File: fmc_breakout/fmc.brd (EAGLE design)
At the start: 101 x 62.3 mm, 19 parts

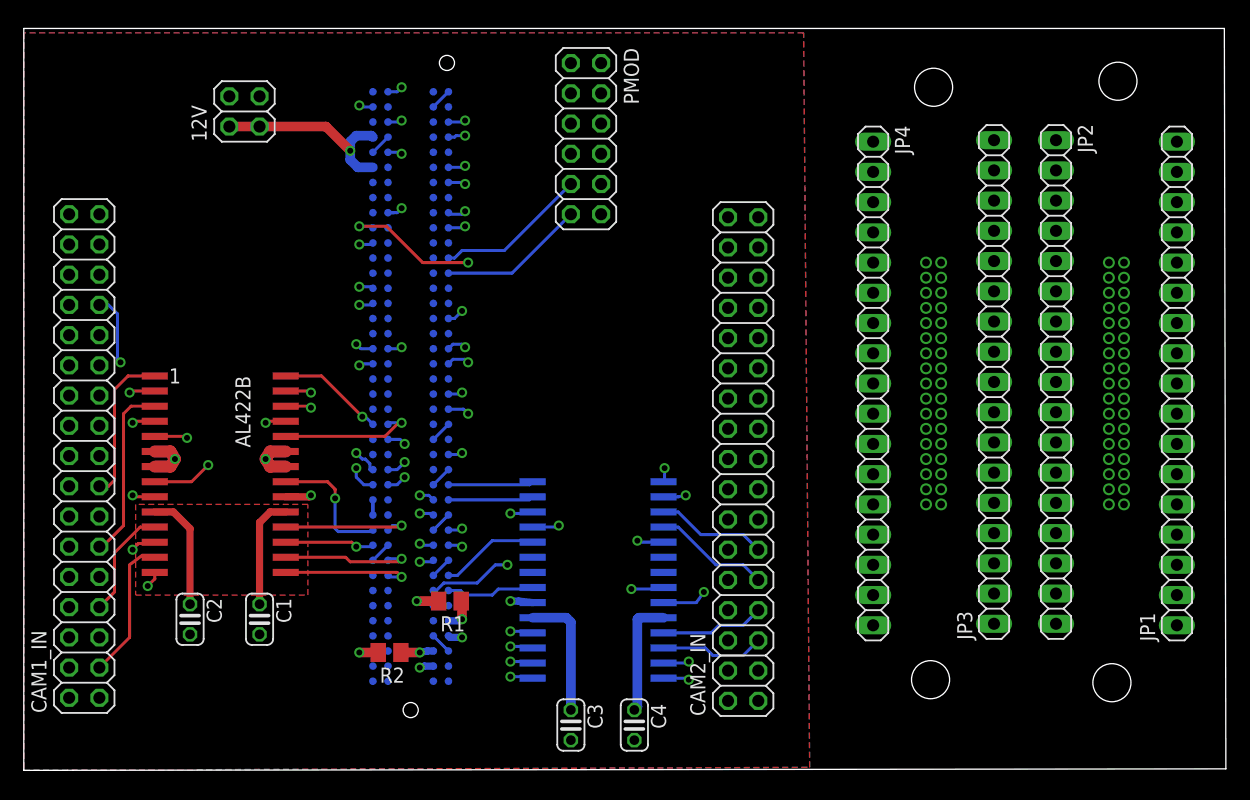
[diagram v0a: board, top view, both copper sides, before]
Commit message: Finished routing traces
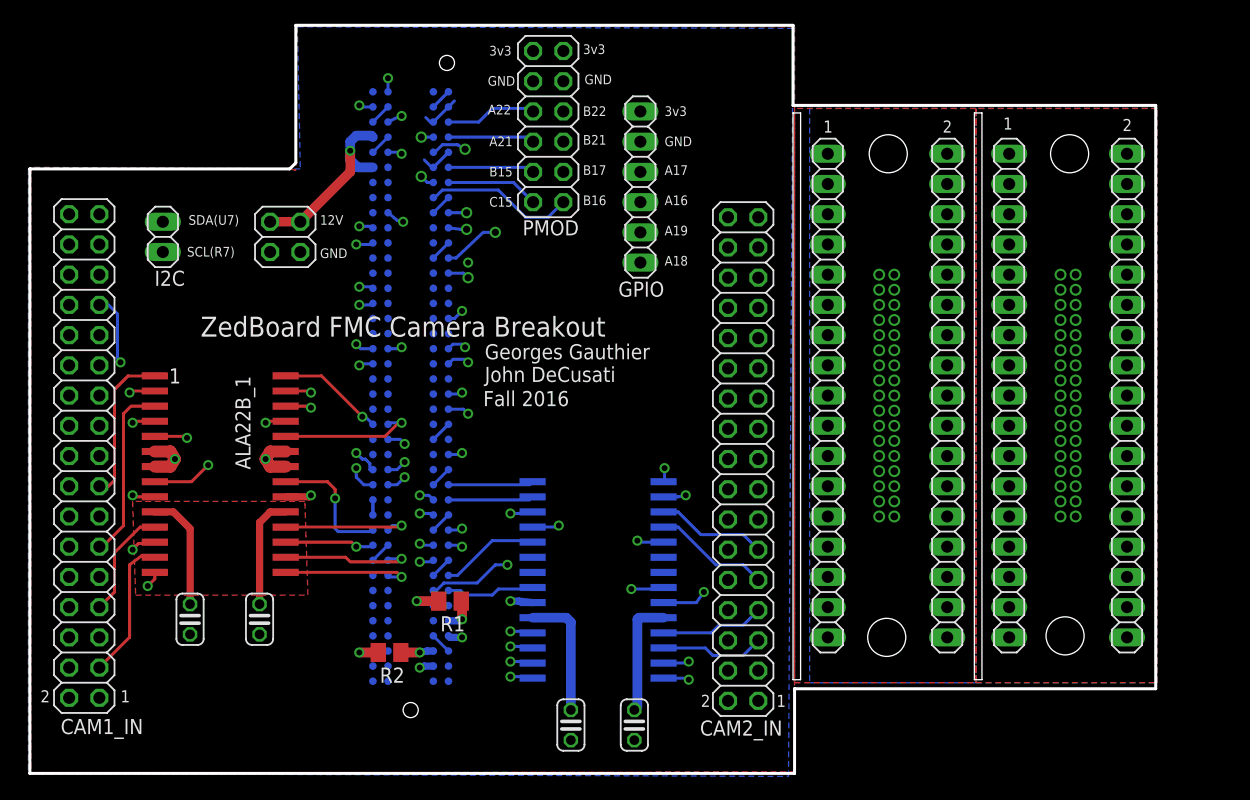
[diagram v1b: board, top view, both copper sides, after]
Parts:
- removed 12V: (no value), pinhead:2X02
- added GPIO: (no value), pinhead:1X06
- added I2C: (no value), pinhead:1X02
- added PWR: PWR, pinhead:2X02
- moved JP1 14.1 mm to (85.3, 36.8), turned to 270 degrees
- moved JP2 6.08 mm to (95.2, 36.8), turned to 90 degrees
- moved CAM1 4.19 mm to (90.3, 36.8), turned to 90 degrees
- moved JP3 4.10 mm to (80.1, 36.8)
- moved CAM2 4.07 mm to (75.1, 36.8)
- moved JP4 3.94 mm to (70.1, 36.8)
- moved PMOD 3.33 mm to (46.6, 59.4)
- renumbered AL422B to ALA22B_1, U$2 to AL422B_2
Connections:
- net 12V: now also PWR.1, PWR.2; no longer 12V.1, 12V.2
- net 3V3: now also GPIO.6
- net A16: now also GPIO.3; no longer PMOD.7
- net A17: now also GPIO.4; no longer PMOD.5
- net A18: now also GPIO.1; no longer PMOD.11
- net A19: now also GPIO.2; no longer PMOD.9
- net A21: now also PMOD.7; no longer PMOD.8
- net A22: now also PMOD.5; no longer PMOD.6
- net B15: now also PMOD.9; no longer PMOD.10
- net B16: now also PMOD.12
- net B17: now also PMOD.10
- net B21: now also PMOD.8
- net B22: now also PMOD.6
- net C15: now also PMOD.11; no longer PMOD.12
- net GND: now also GPIO.5, PWR.3, PWR.4; no longer 12V.3, 12V.4
- net N$40: now also CAM2.25
- net N$60: now also CAM2.20
- net SCL(R7): now also I2C.1
- net SDA(U7): now also I2C.2
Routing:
- net B17: track 0.00 -> 14.1 mm, vias 0 -> 1
- net B22: track 0.00 -> 13.8 mm, vias 0 -> 1
- net N$18: track 0.00 -> 13.0 mm
- net N$1: track 0.00 -> 12.9 mm
- net N$69: track 0.00 -> 12.8 mm
- net N$53: track 0.00 -> 12.8 mm
- net N$35: track 0.00 -> 12.8 mm
- net N$17: track 0.00 -> 12.8 mm
- net N$52: track 0.00 -> 12.7 mm
- net B16: track 0.00 -> 12.7 mm
- net N$19: track 0.00 -> 12.7 mm
- net N$36: track 0.00 -> 12.5 mm
- net N$54: track 0.00 -> 12.4 mm
- net N$34: track 0.00 -> 12.3 mm
- net N$37: track 0.00 -> 12.3 mm
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- added copper zone on layer 1, net N$76
- added copper zone on layer 16, net N$77
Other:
- board size 101 x 62.3 mm -> 94.6 x 62.9 mm
- board text added: "1"
- board text added: "12V"
- board text added: "2"
- board text added: "3v3"
- board text added: "A16"
- board text added: "A17"
- board text added: "A18"
- board text added: "A19"
- board text added: "A21"
- board text added: "A22"
- board text added: "B15"
- board text added: "B16"
- board text added: "B17"
- board text added: "B21"
- board text added: "B22"
- board text added: "C15"
- board text added: "Fall 2016"
- board text added: "GND"
- board text added: "Georges Gauthier"
- board text added: "John DeCusati"
- board text added: "SCL(R7)"
- board text added: "SDA(U7)"
- board text added: "ZedBoard FMC Camera Breakout"

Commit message: FMC board tweaks
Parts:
- moved R2 0.25 mm to (33.3, 15.0)
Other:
- board size 94.6 x 62.9 mm -> 94.6 x 62.1 mm
- board text added: "For LI-VM34LP camera modules & AL422b FIFOs"
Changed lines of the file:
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@@
 <layers>
 <layer number="1" name="Top" color="4" fill="1" visible="yes" active="yes"/>
-<layer number="2" name="Route2" color="13" fill="1" visible="yes" active="yes"/>
+<layer number="2" name="Route2" color="14" fill="1" visible="yes" active="yes"/>
 <layer number="3" name="Route3" color="4" fill="3" visible="no" active="no"/>
 <layer number="14" name="Route14" color="1" fill="6" visible="no" active="no"/>
@@
 <layer number="25" name="tNames" color="7" fill="1" visible="yes" active="yes"/>
 <layer number="26" name="bNames" color="7" fill="1" visible="yes" active="yes"/>
-<layer number="27" name="tValues" color="7" fill="1" visible="yes" active="yes"/>
-<layer number="28" name="bValues" color="7" fill="1" visible="yes" active="yes"/>
+<layer number="27" name="tValues" color="7" fill="1" visible="no" active="yes"/>
+<layer number="28" name="bValues" color="7" fill="1" visible="no" active="yes"/>
 <layer number="29" name="tStop" color="7" fill="3" visible="no" active="yes"/>
 <layer number="30" name="bStop" color="7" fill="6" visible="no" active="yes"/>
@@
 <board>
 <plain>
-<hole x="90.043" y="16.637" drill="3.2"/>
-<hole x="75.184" y="57.15" drill="3.2"/>
-<hole x="75.057" y="16.51" drill="3.2"/>
-<hole x="90.424" y="57.15" drill="3.2"/>
-<wire x1="67.31" y1="5.08" x2="67.31" y2="12.192" width="0.254" layer="20"/>
+<hole x="90.297" y="14.605" drill="3.2"/>
+<hole x="75.184" y="58.674" drill="3.2"/>
+<hole x="75.057" y="14.478" drill="3.2"/>
+<hole x="90.424" y="58.674" drill="3.2"/>
+<wire x1="67.31" y1="5.842" x2="67.31" y2="12.192" width="0.254" layer="20"/>
 <wire x1="67.31" y1="12.192" x2="97.663" y2="12.192" width="0.254" layer="20"/>
 <wire x1="97.663" y1="12.192" x2="97.663" y2="61.214" width="0.254" layer="20"/>
@@
 <text x="27.432" y="51.181" size="0.8128" layer="25" ratio="10">12V</text>
 <text x="27.432" y="48.387" size="0.8128" layer="25" ratio="10">GND</text>
-<text x="41.148" y="35.941" size="1.27" layer="25" ratio="10">Fall 2016</text>
+<text x="41.402" y="35.941" size="1.27" layer="25" ratio="10">Fall 2016</text>
 <text x="10.668" y="11.049" size="1.016" layer="25" ratio="10">1</text>
 <text x="3.937" y="11.049" size="1.016" layer="25" ratio="10">2</text>
 <text x="59.436" y="10.668" size="1.016" layer="25" ratio="10">2</text>
 <text x="65.786" y="10.668" size="1.016" layer="25" ratio="10">1</text>
-<text x="69.723" y="58.928" size="1.016" layer="25" ratio="10">1</text>
-<text x="84.836" y="59.182" size="1.016" layer="25" ratio="10">1</text>
-<text x="79.756" y="58.928" size="1.016" layer="25" ratio="10">2</text>
-<text x="94.869" y="59.055" size="1.016" layer="25" ratio="10">2</text>
+<text x="69.723" y="13.716" size="1.016" layer="25" ratio="10">1</text>
+<text x="85.09" y="13.716" size="1.016" layer="25" ratio="10">1</text>
+<text x="79.756" y="13.716" size="1.016" layer="25" ratio="10">2</text>
+<text x="94.869" y="13.589" size="1.016" layer="25" ratio="10">2</text>
 <wire x1="67.183" y1="67.945" x2="25.4" y2="67.945" width="0.254" layer="20"/>
 <wire x1="25.4" y1="67.945" x2="25.4" y2="56.388" width="0.254" layer="20"/>
 <wire x1="25.4" y1="56.388" x2="24.892" y2="55.88" width="0.254" layer="20"/>
 <wire x1="24.892" y1="55.88" x2="3.048" y2="55.88" width="0.254" layer="20"/>
-<wire x1="3.048" y1="54.356" x2="3.048" y2="5.08" width="0.254" layer="20"/>
-<wire x1="67.31" y1="5.08" x2="3.048" y2="5.08" width="0.254" layer="20"/>
+<wire x1="3.048" y1="54.356" x2="3.048" y2="5.842" width="0.254" layer="20"/>
+<wire x1="67.31" y1="5.842" x2="3.048" y2="5.842" width="0.254" layer="20"/>
 <wire x1="3.048" y1="54.483" x2="3.048" y2="55.88" width="0.254" layer="20"/>
 <text x="16.256" y="48.514" size="0.8128" layer="25" ratio="10">SCL(R7)</text>
+<text x="12.7" y="7.112" size="0.8128" layer="25" ratio="10">For LI-VM34LP camera modules &amp; AL422b FIFOs</text>
 </plain>
 <attributes>
@@
 <attribute name="VALUE" x="51.181" y="12.192" size="1.27" layer="27" ratio="10" rot="R270"/>
 </element>
-<element name="CAM1" library="_hhn_con_pinhead_box_1mm27" package="PHB_1MM27_2X17_SNT" value="" x="90.297" y="36.83" rot="MR90"/>
-<element name="CAM2" library="_hhn_con_pinhead_box_1mm27" package="PHB_1MM27_2X17_SNT" value="" x="75.057" y="36.83" rot="MR90"/>
+<element name="CAM1" library="_hhn_con_pinhead_box_1mm27" package="PHB_1MM27_2X17_SNT" value="" x="90.297" y="36.83" smashed="yes" rot="MR90">
+<attribute name="NAME" x="92.4401" y="20.8439" size="1.27" layer="26" ratio="9" rot="MR0"/>
+<attribute name="VALUE" x="94.5038" y="51.5144" size="1.27" layer="28" ratio="9" rot="MR270"/>
+</element>
+<element name="CAM2" library="_hhn_con_pinhead_box_1mm27" package="PHB_1MM27_2X17_SNT" value="" x="75.057" y="36.83" smashed="yes" rot="MR90">
+<attribute name="NAME" x="77.4541" y="20.8439" size="1.27" layer="26" ratio="9" rot="MR0"/>
+<attribute name="VALUE" x="79.2638" y="51.5144" size="1.27" layer="28" ratio="9" rot="MR270"/>
+</element>
 <element name="JP1" library="pinhead" package="1X17" value="" x="85.344" y="36.83" smashed="yes" rot="R270">
 <attribute name="VALUE" x="82.169" y="58.42" size="1.27" layer="27" rot="R270"/>
@@
 <attribute name="VALUE" x="42.164" y="67.056" size="1.27" layer="27" rot="R270"/>
 </element>
-<element name="R1" library="resistor" package="M0805" value="" x="38.354" y="19.558" rot="R180"/>
-<element name="R2" library="resistor" package="M0805" value="" x="33.274" y="15.24" rot="R180"/>
+<element name="R1" library="resistor" package="M0805" value="" x="38.354" y="19.558" smashed="yes" rot="R180">
+<attribute name="NAME" x="39.624" y="21.844" size="1.27" layer="25" rot="R180"/>
+<attribute name="VALUE" x="39.624" y="22.098" size="1.27" layer="27" rot="R180"/>
+</element>
+<element name="R2" library="resistor" package="M0805" value="" x="33.274" y="14.986" rot="R180"/>
 <element name="I2C" library="pinhead" package="1X02" value="" x="14.224" y="50.165" smashed="yes" rot="R90">
 <attribute name="NAME" x="16.0782" y="47.3202" size="1.27" layer="25" ratio="10" rot="R180"/>
@@
 <wire x1="37.404" y1="19.558" x2="35.56" y2="19.558" width="0.8128" layer="1"/>
 <via x="35.56" y="19.558" extent="1-16" drill="0.5" shape="octagon"/>
-<wire x1="32.324" y1="15.24" x2="30.734" y2="15.24" width="0.8128" layer="1"/>
-<via x="30.734" y="15.24" extent="1-16" drill="0.5" shape="octagon"/>
+<wire x1="32.324" y1="14.986" x2="30.734" y2="14.986" width="0.8128" layer="1"/>
+<via x="30.734" y="14.986" extent="1-16" drill="0.5" shape="octagon"/>
 <wire x1="36.957" y1="59.817" x2="38.227" y2="61.087" width="0.254" layer="16"/>
 <wire x1="36.957" y1="59.817" x2="36.703" y2="59.817" width="0.254" layer="16"/>
@@
 <polygon width="0.254" layer="16" isolate="0.4064">
 <vertex x="2.921" y="55.88"/>
-<vertex x="2.921" y="5.08"/>
-<vertex x="66.802" y="4.826"/>
+<vertex x="3.175" y="6.604"/>
+<vertex x="67.056" y="6.35"/>
 <vertex x="67.183" y="67.691"/>
 <vertex x="25.527" y="67.818"/>
@@
 <wire x1="41.91" y1="19.05" x2="42.418" y2="19.558" width="0.6096" layer="2"/>
 <contactref element="R2" pad="1"/>
-<wire x1="34.224" y1="15.24" x2="35.814" y2="15.24" width="0.8128" layer="1"/>
+<wire x1="34.224" y1="14.986" x2="35.814" y2="15.24" width="0.8128" layer="1"/>
 </signal>
 <signal name="M19">
@@
 <vertex x="24.892" y="55.88"/>
 <vertex x="3.175" y="56.007"/>
-<vertex x="3.175" y="5.08"/>
-<vertex x="67.31" y="5.207"/>
+<vertex x="3.175" y="6.35"/>
+<vertex x="67.31" y="6.477"/>
 <vertex x="67.31" y="67.818"/>
 <vertex x="25.527" y="67.945"/>
